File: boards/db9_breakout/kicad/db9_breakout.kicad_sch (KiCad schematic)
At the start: 23 parts, among them J1 DE9_Pins, J2 DE9_Socket, J3 Screw_Terminal_01x09, J4 Screw_Terminal_01x09, J5 Conn_02x10_Row_Letter_First

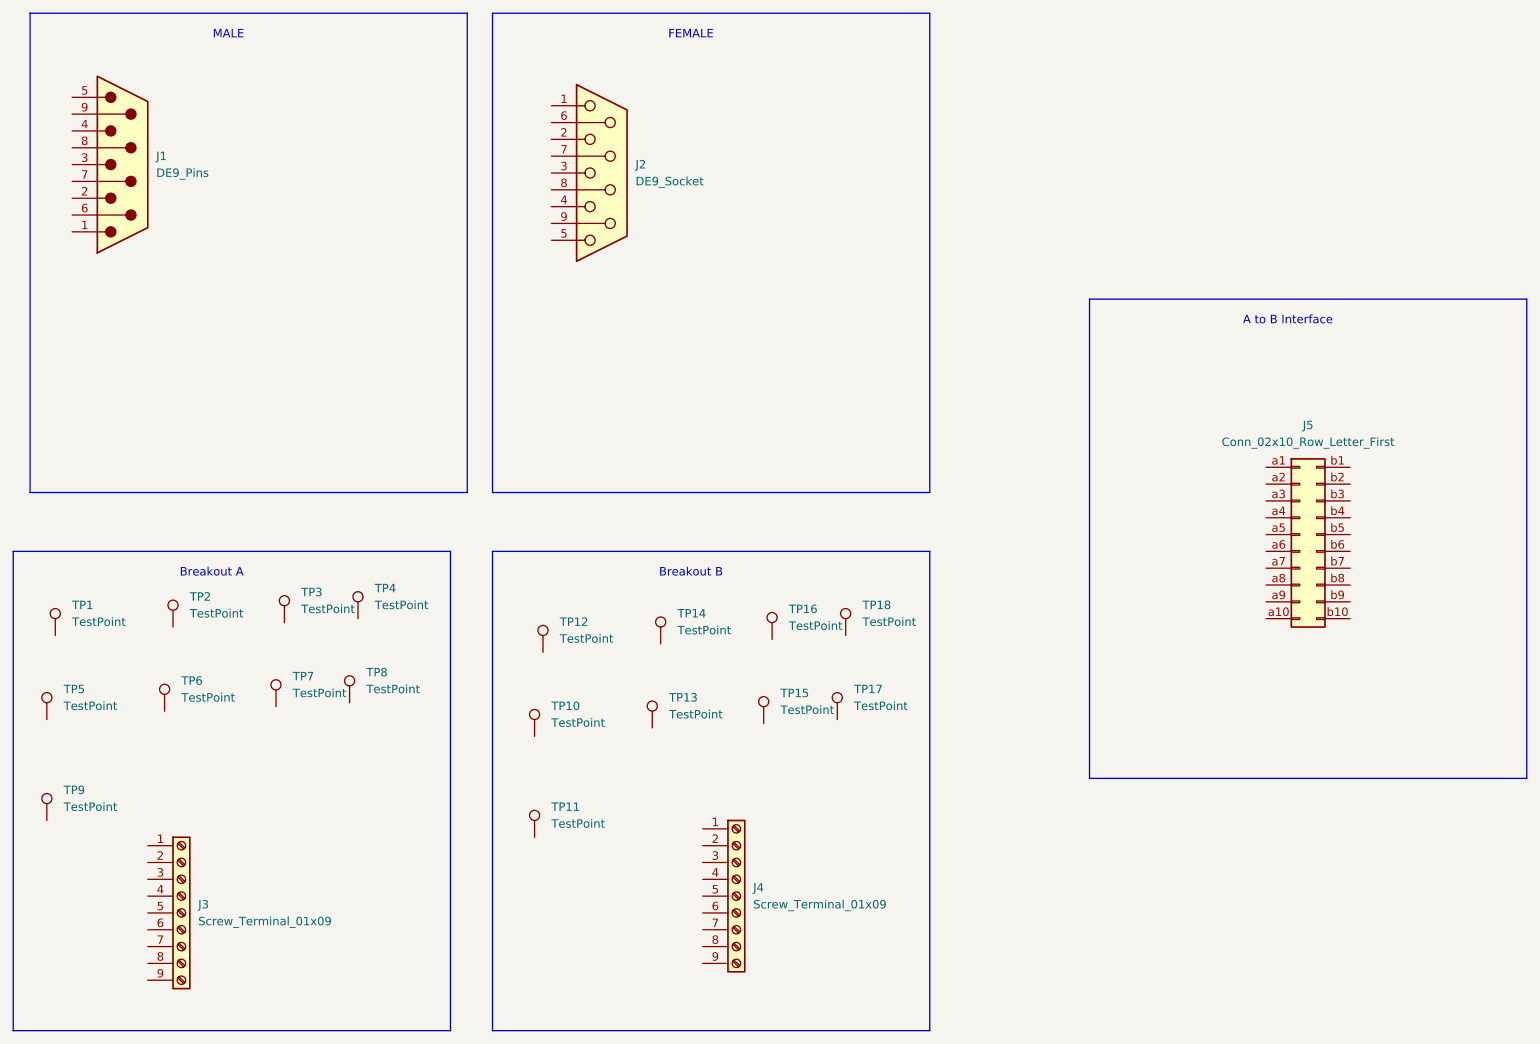
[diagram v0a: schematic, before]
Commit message: schematic finished, need footprint assignment
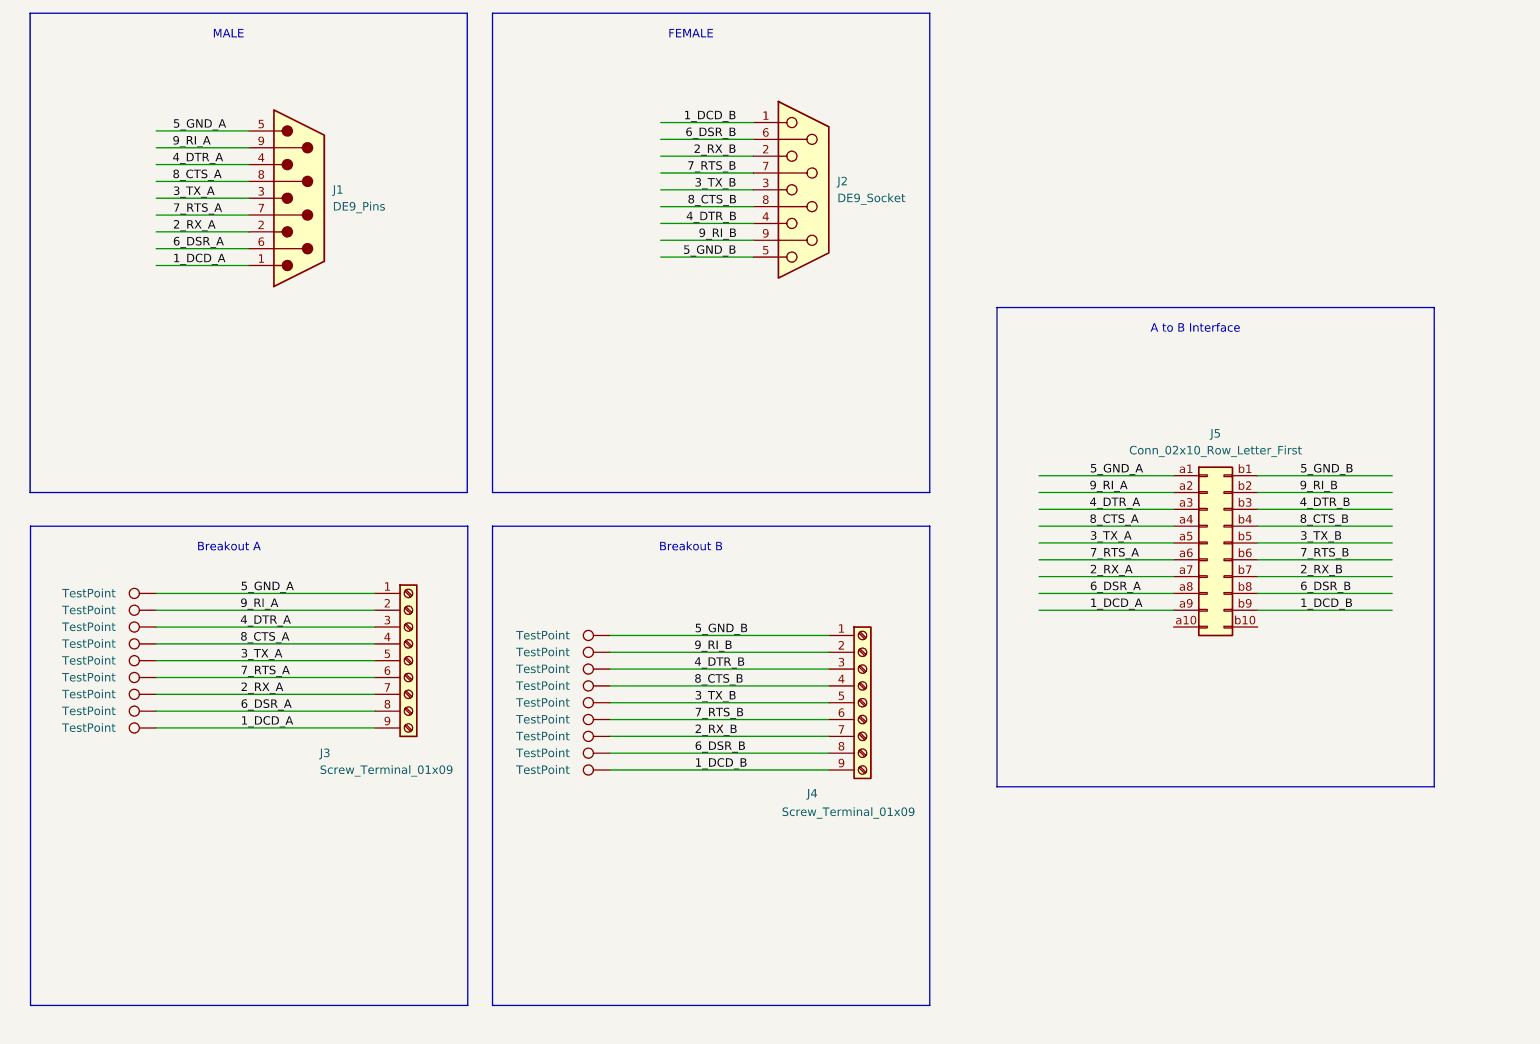
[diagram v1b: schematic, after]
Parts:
- removed TP10, TP11, TP12, TP13, TP14, TP15, TP16, TP17, TP18, TP2, TP3, TP4, TP5, TP6, TP7, TP8, TP9: TestPoint, symbol Connector:TestPoint
- added 5_GND_A1, 5_GND_A10, 5_GND_A11, 5_GND_A12, 5_GND_A13, 5_GND_A14, 5_GND_A15, 5_GND_A16, 5_GND_A17, 5_GND_A2, 5_GND_A3, 5_GND_A4, 5_GND_A5, 5_GND_A6, 5_GND_A7, 5_GND_A8, 5_GND_A9: TestPoint, symbol Connector:TestPoint
- renumbered TP1 to 5_GND_A
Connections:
- net 5_GND_A: now reaches 5_GND_A.1
- net 5_GND_A: now also J1.5, J3.1 (Pin_1), J5.a1 (Pin_a1)
- net 9_RI_A: now reaches J3.2 (Pin_2)
- net 9_RI_A: now also J1.9, J5.a2 (Pin_a2), 5_GND_A1.1
- net 4_DTR_A: now reaches J3.3 (Pin_3)
- net 4_DTR_A: now also J1.4, J5.a3 (Pin_a3), 5_GND_A2.1
- net 8_CTS_A: now reaches J3.4 (Pin_4)
- net 8_CTS_A: now also J1.8, J5.a4 (Pin_a4), 5_GND_A3.1
- net 3_TX_A: now reaches J3.5 (Pin_5)
- net 3_TX_A: now also J1.3, J5.a5 (Pin_a5), 5_GND_A4.1
- net 7_RTS_A: now reaches J3.6 (Pin_6)
- net 7_RTS_A: now also J1.7, J5.a6 (Pin_a6), 5_GND_A5.1
- net 2_RX_A: now reaches J3.7 (Pin_7)
- net 2_RX_A: now also J1.2, J5.a7 (Pin_a7), 5_GND_A6.1
- net 6_DSR_A: now reaches J3.8 (Pin_8)
- net 6_DSR_A: now also J1.6, J5.a8 (Pin_a8), 5_GND_A7.1
- net 1_DCD_A: now reaches J3.9 (Pin_9)
- net 1_DCD_A: now also J1.1, J5.a9 (Pin_a9), 5_GND_A8.1
- net 5_GND_B: now reaches J4.1 (Pin_1)
- net 5_GND_B: now also J2.5, J5.b1 (Pin_b1), 5_GND_A9.1
- net 9_RI_B: now reaches J4.2 (Pin_2)
- net 9_RI_B: now also J2.9, J5.b2 (Pin_b2), 5_GND_A10.1
- net 4_DTR_B: now reaches J4.3 (Pin_3)
- net 4_DTR_B: now also J2.4, J5.b3 (Pin_b3), 5_GND_A11.1
- net 8_CTS_B: now reaches J4.4 (Pin_4)
- net 8_CTS_B: now also J2.8, J5.b4 (Pin_b4), 5_GND_A12.1
- net 3_TX_B: now reaches J4.5 (Pin_5)
- net 3_TX_B: now also J2.3, J5.b5 (Pin_b5), 5_GND_A13.1
- net 7_RTS_B: now reaches J4.6 (Pin_6)
- net 7_RTS_B: now also J2.7, J5.b6 (Pin_b6), 5_GND_A14.1
- net 2_RX_B: now reaches J4.7 (Pin_7)
- net 2_RX_B: now also J2.2, J5.b7 (Pin_b7), 5_GND_A15.1
- net 6_DSR_B: now reaches J4.8 (Pin_8)
- net 6_DSR_B: now also J2.6, J5.b8 (Pin_b8), 5_GND_A16.1
- net 1_DCD_B: now reaches J4.9 (Pin_9)
- net 1_DCD_B: now also J2.1, J5.b9 (Pin_b9), 5_GND_A17.1
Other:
- moved on the sheet: J1, J2, J3, J4, J5

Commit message: footprint assigned, board started
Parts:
- removed 5_GND_A: TestPoint, symbol Connector:TestPoint
- added 5_GND_A18: TestPoint, TestPoint:TestPoint_Loop_D2.60mm_Drill1.6mm_Beaded, symbol Connector:TestPoint
- 5_GND_A1, 5_GND_A10, 5_GND_A11, 5_GND_A12, 5_GND_A13, 5_GND_A14, 5_GND_A15, 5_GND_A16, 5_GND_A17, 5_GND_A2, 5_GND_A3, 5_GND_A4, 5_GND_A5, 5_GND_A6, 5_GND_A7, 5_GND_A8, 5_GND_A9: footprint (none) -> TestPoint:TestPoint_Loop_D2.60mm_Drill1.6mm_Beaded
- J1: footprint (none) -> Connector_Dsub:DSUB-9_Pins_Horizontal_P2.77x2.84mm_EdgePinOffset9.40mm
- J2: footprint (none) -> Connector_Dsub:DSUB-9_Socket_Horizontal_P2.77x2.84mm_EdgePinOffset9.40mm
- J3, J4: footprint (none) -> TerminalBlock_Phoenix:TerminalBlock_Phoenix_MKDS-1,5-9-5.08_1x09_P5.08mm_Horizontal
- J5: footprint (none) -> Connector_PinHeader_2.54mm:PinHeader_2x10_P2.54mm_Vertical
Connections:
- net 5_GND_A: now also 5_GND_A18.1
- no-connect marks 0 -> 2
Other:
- moved on the sheet: J2
